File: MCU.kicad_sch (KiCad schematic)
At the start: 22 parts, among them U1 LTV-817, U2 LTV-817, Y1 TXC 7R-32.000MEEV-T

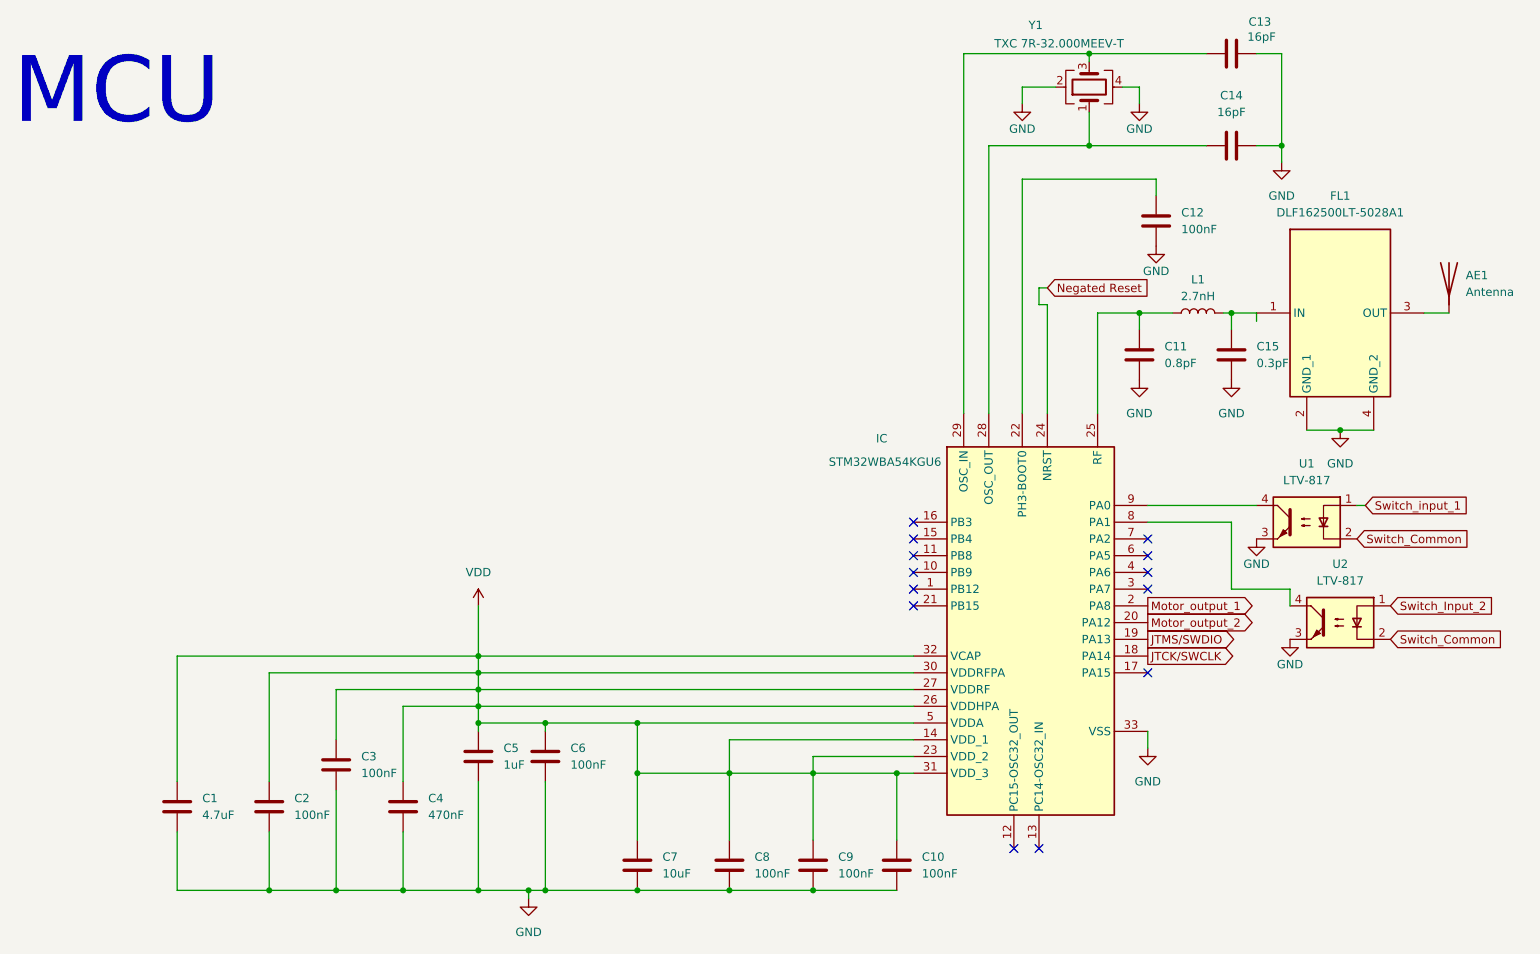
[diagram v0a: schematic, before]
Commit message: połączenie ścieżkami, wylanie masy
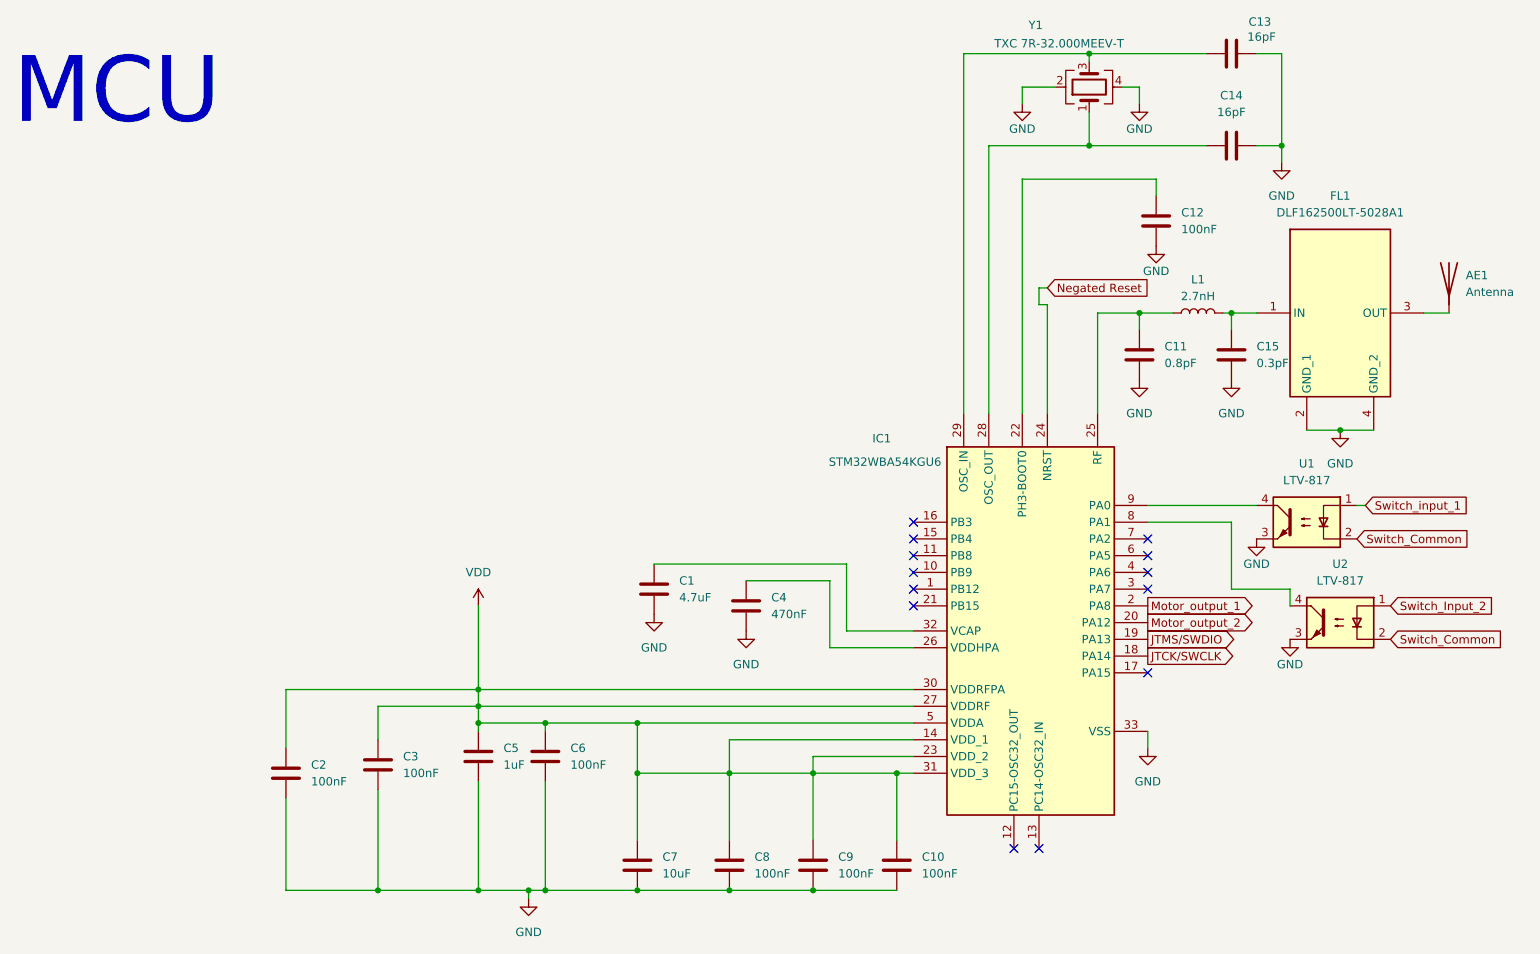
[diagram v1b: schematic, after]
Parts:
- AE1: footprint (none) -> RF_Antenna:Texas_SWRA117D_2.4GHz_Right
- C1, C10, C11, C12, C13, C14, C15, C2, C3, C4, C5, C6, C7, C8, C9: footprint Capacitor_SMD:C_0201_0603Metric -> Capacitor_SMD:C_0603_1608Metric_Pad1.08x0.95mm_HandSolder
- IC1: renamed from 111111111; Reference_1 IC -> IC1
- L1: footprint Inductor_SMD:L_0201_0603Metric -> Inductor_SMD:L_0603_1608Metric_Pad1.05x0.95mm_HandSolder
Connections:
- net VDD: no longer C1.1, C4.1, IC1.26 (VDDHPA), IC1.32 (VCAP)
- new net: C4.1, IC1.26 (VDDHPA)
- new net: C1.1, IC1.32 (VCAP)
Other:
- moved on the sheet: C1, C2, C3, C4

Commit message: poprawka wymiaru płytki
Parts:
- U1, U2: footprint Package_DIP:DIP-4_W7.62mm -> Package_DIP:SMDIP-4_W9.53mm; symbol Isolator:LTV-817 -> Isolator:LTV-817S
- renumbered C2 to C1, C3 to C2, C5 to C3, C6 to C4, C7 to C5, C1 to C6, C8 to C7, C4 to C8
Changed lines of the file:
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@@
 		(on_board yes)
 		(dnp no)
-		(property "Reference" "#PWR07"
+		(property "Reference" "#PWR09"
 			(at 196.85 55.88 0)
 			(effects
@@
 			(project "sterownik_rolety_Zigbee"
 				(path "/e63e39d7-6ac0-4ffd-8aa3-1841a4541b55/f5ed516b-1078-4b27-8310-468dae8763f9"
-					(reference "#PWR07")
+					(reference "#PWR09")
 					(unit 1)
 				)
@@
 		(dnp no)
 		(fields_autoplaced yes)
-		(property "Reference" "C5"
+		(property "Reference" "C3"
 			(at 97.79 125.7299 0)
 			(effects
@@
 			(project "sterownik_rolety_Zigbee"
 				(path "/e63e39d7-6ac0-4ffd-8aa3-1841a4541b55/f5ed516b-1078-4b27-8310-468dae8763f9"
-					(reference "C5")
+					(reference "C3")
 					(unit 1)
 				)
@@
 		(dnp no)
 		(fields_autoplaced yes)
-		(property "Reference" "C4"
+		(property "Reference" "C8"
 			(at 138.43 102.8699 0)
 			(effects
@@
 			(project "sterownik_rolety_Zigbee"
 				(path "/e63e39d7-6ac0-4ffd-8aa3-1841a4541b55/f5ed516b-1078-4b27-8310-468dae8763f9"
-					(reference "C4")
+					(reference "C8")
 					(unit 1)
 				)
@@
 		(on_board yes)
 		(dnp no)
-		(property "Reference" "#PWR011"
+		(property "Reference" "#PWR013"
 			(at 217.17 115.57 0)
 			(effects
@@
 			(project "sterownik_rolety_Zigbee"
 				(path "/e63e39d7-6ac0-4ffd-8aa3-1841a4541b55/f5ed516b-1078-4b27-8310-468dae8763f9"
-					(reference "#PWR011")
+					(reference "#PWR013")
 					(unit 1)
 				)
@@
 		(dnp no)
 		(fields_autoplaced yes)
-		(property "Reference" "#PWR06"
+		(property "Reference" "#PWR08"
 			(at 195.58 132.08 0)
 			(effects
@@
 			(project ""
 				(path "/e63e39d7-6ac0-4ffd-8aa3-1841a4541b55/f5ed516b-1078-4b27-8310-468dae8763f9"
-					(reference "#PWR06")
+					(reference "#PWR08")
 					(unit 1)
 				)
@@
 		(dnp no)
 		(fields_autoplaced yes)
-		(property "Reference" "#PWR05"
+		(property "Reference" "#PWR07"
 			(at 194.31 76.2 0)
 			(effects
@@
 			(project ""
 				(path "/e63e39d7-6ac0-4ffd-8aa3-1841a4541b55/f5ed516b-1078-4b27-8310-468dae8763f9"
-					(reference "#PWR05")
+					(reference "#PWR07")
 					(unit 1)
 				)
@@
 		(dnp no)
 		(fields_autoplaced yes)
-		(property "Reference" "C2"
+		(property "Reference" "C1"
 			(at 68.58 128.2699 0)
 			(effects
@@
 			(project "sterownik_rolety_Zigbee"
 				(path "/e63e39d7-6ac0-4ffd-8aa3-1841a4541b55/f5ed516b-1078-4b27-8310-468dae8763f9"
-					(reference "C2")
+					(reference "C1")
 					(unit 1)
 				)
@@
 		(dnp no)
 		(fields_autoplaced yes)
-		(property "Reference" "C1"
+		(property "Reference" "C6"
 			(at 124.46 100.3299 0)
 			(effects
@@
 			(project "sterownik_rolety_Zigbee"
 				(path "/e63e39d7-6ac0-4ffd-8aa3-1841a4541b55/f5ed516b-1078-4b27-8310-468dae8763f9"
-					(reference "C1")
+					(reference "C6")
 					(unit 1)
 				)
@@
 		(dnp no)
 		(fields_autoplaced yes)
-		(property "Reference" "C7"
+		(property "Reference" "C5"
 			(at 121.92 142.2399 0)
 			(effects
@@
 			(project "sterownik_rolety_Zigbee"
 				(path "/e63e39d7-6ac0-4ffd-8aa3-1841a4541b55/f5ed516b-1078-4b27-8310-468dae8763f9"
-					(reference "C7")
+					(reference "C5")
 					(unit 1)
 				)
@@
 		(on_board yes)
 		(dnp no)
-		(property "Reference" "#PWR04"
+		(property "Reference" "#PWR06"
 			(at 194.31 34.29 0)
 			(effects
@@
 			(project "sterownik_rolety_Zigbee"
 				(path "/e63e39d7-6ac0-4ffd-8aa3-1841a4541b55/f5ed516b-1078-4b27-8310-468dae8763f9"
-					(reference "#PWR04")
+					(reference "#PWR06")
 					(unit 1)
 				)
@@
 	)
 	(symbol
-		(lib_id "Isolator:LTV-817")
+		(lib_id "Isolator:LTV-817S")
 		(at 224.79 106.68 0)
 		(mirror y)
@@
 			)
 		)
-		(property "Footprint" "Package_DIP:DIP-4_W7.62mm"
-			(at 229.87 111.76 0)
-			(effects
-				(font
-					(size 1.27 1.27)
-					(italic yes)
-				)
-				(justify left)
+		(property "Footprint" "Package_DIP:SMDIP-4_W9.53mm"
+			(at 224.79 114.3 0)
+			(effects
+				(font
+					(size 1.27 1.27)
+				)
 				(hide yes)
 			)
 		)
 		(property "Datasheet" "http://www.us.liteon.com/downloads/LTV-817-827-847.PDF"
-			(at 224.79 109.22 0)
-			(effects
-				(font
-					(size 1.27 1.27)
-				)
-				(justify left)
-				(hide yes)
-			)
-		)
-		(property "Description" "DC Optocoupler, Vce 35V, CTR 50%, DIP-4"
+			(at 233.68 99.06 0)
+			(effects
+				(font
+					(size 1.27 1.27)
+				)
+				(hide yes)
+			)
+		)
+		(property "Description" "DC Optocoupler, Vce 35V, CTR 50%, SMDIP-4"
 			(at 224.79 106.68 0)
 			(effects
@@
 		(dnp no)
 		(fields_autoplaced yes)
-		(property "Reference" "C8"
+		(property "Reference" "C7"
 			(at 135.89 142.2399 0)
 			(effects
@@
 			(project "sterownik_rolety_Zigbee"
 				(path "/e63e39d7-6ac0-4ffd-8aa3-1841a4541b55/f5ed516b-1078-4b27-8310-468dae8763f9"
-					(reference "C8")
+					(reference "C7")
 					(unit 1)
 				)
@@
 		(on_board yes)
 		(dnp no)
-		(property "Reference" "#PWR03"
+		(property "Reference" "#PWR05"
 			(at 176.53 34.29 0)
 			(effects
@@
 			(project "sterownik_rolety_Zigbee"
 				(path "/e63e39d7-6ac0-4ffd-8aa3-1841a4541b55/f5ed516b-1078-4b27-8310-468dae8763f9"
-					(reference "#PWR03")
+					(reference "#PWR05")
 					(unit 1)
 				)
@@
 		(dnp no)
 		(fields_autoplaced yes)
-		(property "Reference" "C3"
+		(property "Reference" "C2"
 			(at 82.55 126.9999 0)
 			(effects
@@
 			(project "sterownik_rolety_Zigbee"
 				(path "/e63e39d7-6ac0-4ffd-8aa3-1841a4541b55/f5ed516b-1078-4b27-8310-468dae8763f9"
-					(reference "C3")
+					(reference "C2")
 					(unit 1)
 				)
@@
 		(dnp no)
 		(fields_autoplaced yes)
-		(property "Reference" "#PWR012"
+		(property "Reference" "#PWR014"
 			(at 224.79 83.82 0)
 			(effects
@@
 			(project ""
 				(path "/e63e39d7-6ac0-4ffd-8aa3-1841a4541b55/f5ed516b-1078-4b27-8310-468dae8763f9"
-					(reference "#PWR012")
+					(reference "#PWR014")
 					(unit 1)
 				)
@@
 		(dnp no)
 		(fields_autoplaced yes)
-		(property "Reference" "#PWR010"
+		(property "Reference" "#PWR012"
 			(at 215.9 43.18 0)
 			(effects
@@
 			(project "sterownik_rolety_Zigbee"
 				(path "/e63e39d7-6ac0-4ffd-8aa3-1841a4541b55/f5ed516b-1078-4b27-8310-468dae8763f9"
-					(reference "#PWR010")
+					(reference "#PWR012")
 					(unit 1)
 				)
@@
 		(on_board yes)
 		(dnp no)
-		(property "Reference" "#PWR09"
+		(property "Reference" "#PWR011"
 			(at 212.09 100.33 0)
 			(effects
@@
 			(project "sterownik_rolety_Zigbee"
 				(path "/e63e39d7-6ac0-4ffd-8aa3-1841a4541b55/f5ed516b-1078-4b27-8310-468dae8763f9"
-					(reference "#PWR09")
+					(reference "#PWR011")
 					(unit 1)
 				)
@@
 		(dnp no)
 		(fields_autoplaced yes)
-		(property "Reference" "C6"
+		(property "Reference" "C4"
 			(at 107.95 125.7299 0)
 			(effects
@@
 			(project "sterownik_rolety_Zigbee"
 				(path "/e63e39d7-6ac0-4ffd-8aa3-1841a4541b55/f5ed516b-1078-4b27-8310-468dae8763f9"
-					(reference "C6")
-					(unit 1)
-				)
-			)
-		)
-	)
-	(symbol
-		(lib_id "Isolator:LTV-817")
+					(reference "C4")
+					(unit 1)
+				)
+			)
+		)
+	)
+	(symbol
+		(lib_id "Isolator:LTV-817S")
 		(at 219.71 91.44 0)
 		(mirror y)
@@
 			)
 		)
-		(property "Footprint" "Package_DIP:DIP-4_W7.62mm"
-			(at 224.79 96.52 0)
-			(effects
-				(font
-					(size 1.27 1.27)
-					(italic yes)
-				)
-				(justify left)
+		(property "Footprint" "Package_DIP:SMDIP-4_W9.53mm"
+			(at 219.71 99.06 0)
+			(effects
+				(font
+					(size 1.27 1.27)
+				)
 				(hide yes)
 			)
 		)
 		(property "Datasheet" "http://www.us.liteon.com/downloads/LTV-817-827-847.PDF"
-			(at 219.71 93.98 0)
-			(effects
-				(font
-					(size 1.27 1.27)
-				)
-				(justify left)
-				(hide yes)
-			)
-		)
-		(property "Description" "DC Optocoupler, Vce 35V, CTR 50%, DIP-4"
+			(at 228.6 83.82 0)
+			(effects
+				(font
+					(size 1.27 1.27)
+				)
+				(hide yes)
+			)
+		)
+		(property "Description" "DC Optocoupler, Vce 35V, CTR 50%, SMDIP-4"
 			(at 219.71 91.44 0)
 			(effects
@@
 		(dnp no)
 		(fields_autoplaced yes)
-		(property "Reference" "#PWR020"
+		(property "Reference" "#PWR04"
 			(at 134.62 114.3 0)
 			(effects
@@
 			(project "sterownik_rolety_Zigbee"
 				(path "/e63e39d7-6ac0-4ffd-8aa3-1841a4541b55/f5ed516b-1078-4b27-8310-468dae8763f9"
-					(reference "#PWR020")
+					(reference "#PWR04")
 					(unit 1)
 				)
@@
 		(dnp no)
 		(fields_autoplaced yes)
-		(property "Reference" "#PWR08"
+		(property "Reference" "#PWR010"
 			(at 208.28 76.2 0)
 			(effects
@@
 			(project ""
 				(path "/e63e39d7-6ac0-4ffd-8aa3-1841a4541b55/f5ed516b-1078-4b27-8310-468dae8763f9"
-					(reference "#PWR08")
+					(reference "#PWR010")
 					(unit 1)
 				)
@@
 		(dnp no)
 		(fields_autoplaced yes)
-		(property "Reference" "#PWR019"
+		(property "Reference" "#PWR03"
 			(at 120.65 111.76 0)
 			(effects
@@
 			(project "sterownik_rolety_Zigbee"
 				(path "/e63e39d7-6ac0-4ffd-8aa3-1841a4541b55/f5ed516b-1078-4b27-8310-468dae8763f9"
-					(reference "#PWR019")
-					(unit 1)
-				)
+					(reference "#PWR03")
+					(unit 1)
+				)
